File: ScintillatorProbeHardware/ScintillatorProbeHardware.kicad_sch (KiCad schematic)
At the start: 65 parts, among them J1 USB_B, Q1 BUX87, Q2 Q_NPN_BCE, Q3 Q_NPN_BCE, T1 24:1800, U1 ICL7660, U2 LM4562, U3 LM358, U4 STM32F103C8Tx

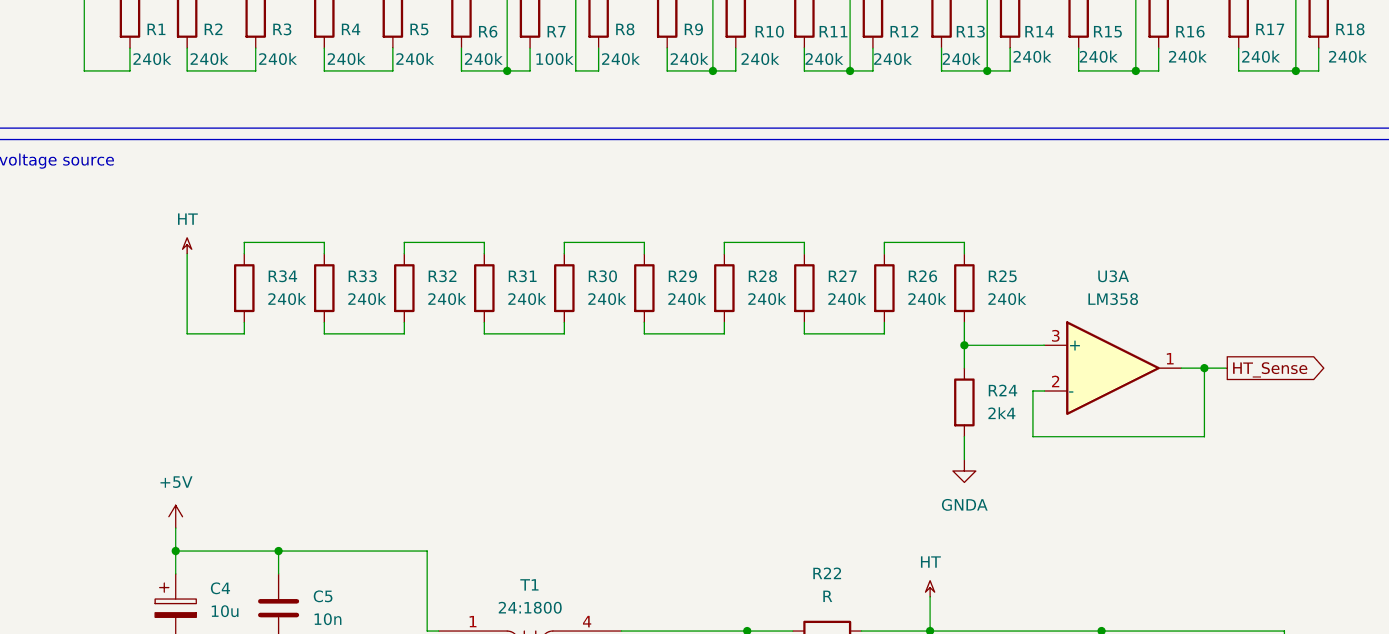
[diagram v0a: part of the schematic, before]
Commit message: USB interface working; Command parser; PWM generator
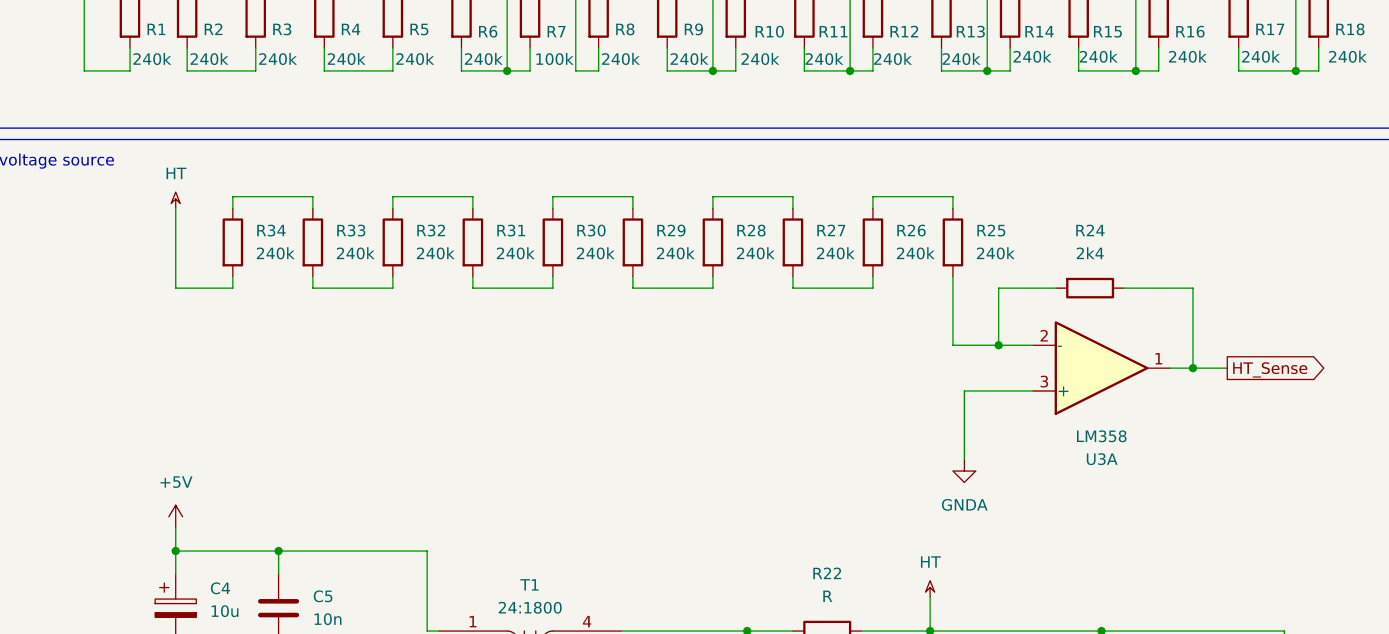
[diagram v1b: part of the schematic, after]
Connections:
- net GNDA: now also U3.3 (+); no longer R24.2
- net HT_Sense: now also R24.1; no longer U3.2 (-)
- new net: R24.2, R25.2, U3.2 (-)
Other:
- moved on the sheet: R24, R25, R26, R27, R28, R29, R30, R31, R32, R33, R34, U3A

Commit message: ...
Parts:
- removed Q2: Q_NPN_BCE, symbol Device:Q_NPN_BCE
- added Q2: BC546A, symbol Device:Q_NPN_CBE
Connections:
- net at R35.2: now also Q2.2 (B)
- net at Q1.2 (C), T1.2 (AB): now also Q2.1 (C)
- net at Q1.1 (B): now also Q2.3 (E)
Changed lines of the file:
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@@
 	)
 	(symbol
-		(lib_id "Device:Q_NPN_BCE")
-		(at 55.88 152.4 0)
-		(unit 1)
-		(exclude_from_sim no)
-		(in_bom yes)
-		(on_board yes)
-		(dnp no)
-		(fields_autoplaced yes)
-		(property "Reference" "Q2"
-			(at 60.96 151.1299 0)
-			(effects
-				(font
-					(size 1.27 1.27)
-				)
-				(justify left)
-			)
-		)
-		(property "Value" "Q_NPN_BCE"
-			(at 60.96 153.6699 0)
-			(effects
-				(font
-					(size 1.27 1.27)
-				)
-				(justify left)
-			)
-		)
-		(property "Footprint" ""
-			(at 60.96 149.86 0)
-			(effects
-				(font
-					(size 1.27 1.27)
-				)
-				(hide yes)
-			)
-		)
-		(property "Datasheet" "~"
-			(at 55.88 152.4 0)
-			(effects
-				(font
-					(size 1.27 1.27)
-				)
-				(hide yes)
-			)
-		)
-		(property "Description" "NPN transistor, base/collector/emitter"
-			(at 55.88 152.4 0)
-			(effects
-				(font
-					(size 1.27 1.27)
-				)
-				(hide yes)
-			)
-		)
-		(pin "3"
-		)
-		(pin "1"
-		)
-		(pin "2"
-		)
-		(instances
-			(project ""
-				(path "/b577c016-7a5f-4050-822e-6f81bc7c5cda"
-					(reference "Q2")
-					(unit 1)
-				)
-			)
-		)
-	)
-	(symbol
 		(lib_id "Amplifier_Operational:LM4562")
 		(at 266.7 66.04 0)
@@
 					(unit 1)
 				)
+			)
+		)
+	)
+	(symbol
+		(lib_id "Device:Q_NPN_CBE")
+		(at 55.88 152.4 0)
+		(unit 1)
+		(exclude_from_sim no)
+		(in_bom yes)
+		(on_board yes)
+		(dnp no)
+		(fields_autoplaced yes)
+		(property "Reference" "Q2"
+			(at 60.96 151.1299 0)
+			(effects
+				(font
+					(size 1.27 1.27)
+				)
+				(justify left)
+			)
+		)
+		(property "Value" "BC546A"
+			(at 60.96 153.6699 0)
+			(effects
+				(font
+					(size 1.27 1.27)
+				)
+				(justify left)
+			)
+		)
+		(property "Footprint" ""
+			(at 60.96 149.86 0)
+			(effects
+				(font
+					(size 1.27 1.27)
+				)
+				(hide yes)
+			)
+		)
+		(property "Datasheet" "~"
+			(at 55.88 152.4 0)
+			(effects
+				(font
+					(size 1.27 1.27)
+				)
+				(hide yes)
+			)
+		)
+		(property "Description" "NPN transistor, collector/base/emitter"
+			(at 55.88 152.4 0)
+			(effects
+				(font
+					(size 1.27 1.27)
+				)
+				(hide yes)
+			)
+		)
+		(pin "1"
+		)
+		(pin "2"
+		)
+		(pin "3"
+		)
+		(instances
+			(project ""
+				(path "/b577c016-7a5f-4050-822e-6f81bc7c5cda"
+					(reference "Q2")
+					(unit 1)
+				)

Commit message: Flyback driving circuit changed to NMOS
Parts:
- removed Q1: BUX87, symbol Device:Q_NPN_BCE
- added D5, D6: D_Schottky, symbol Device:D_Schottky
- added Q1: Q_NMOS_GDS, symbol Device:Q_NMOS_GDS
- added R37: 330R, symbol Device:R
- added R38: 1k, symbol Device:R
- C8: value C -> 1n
- R35: value R -> 330R
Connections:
- net +3.3V: now also D5.1 (K), R37.1
- net GND: now also Q2.3 (E), Q1.3 (S)
- net GNDA: now also D6.2 (A)
- net HT_Sense: now also D5.2 (A), D6.1 (K), R38.2; no longer R24.1, U3.1
- net at Q2.1 (C): now also Q1.1 (G), R37.2; no longer T1.2 (AB)
- new net: R24.1, R38.1, U3.1
- new net: Q1.2 (D), T1.2 (AB)
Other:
- moved on the sheet: Q2, R35

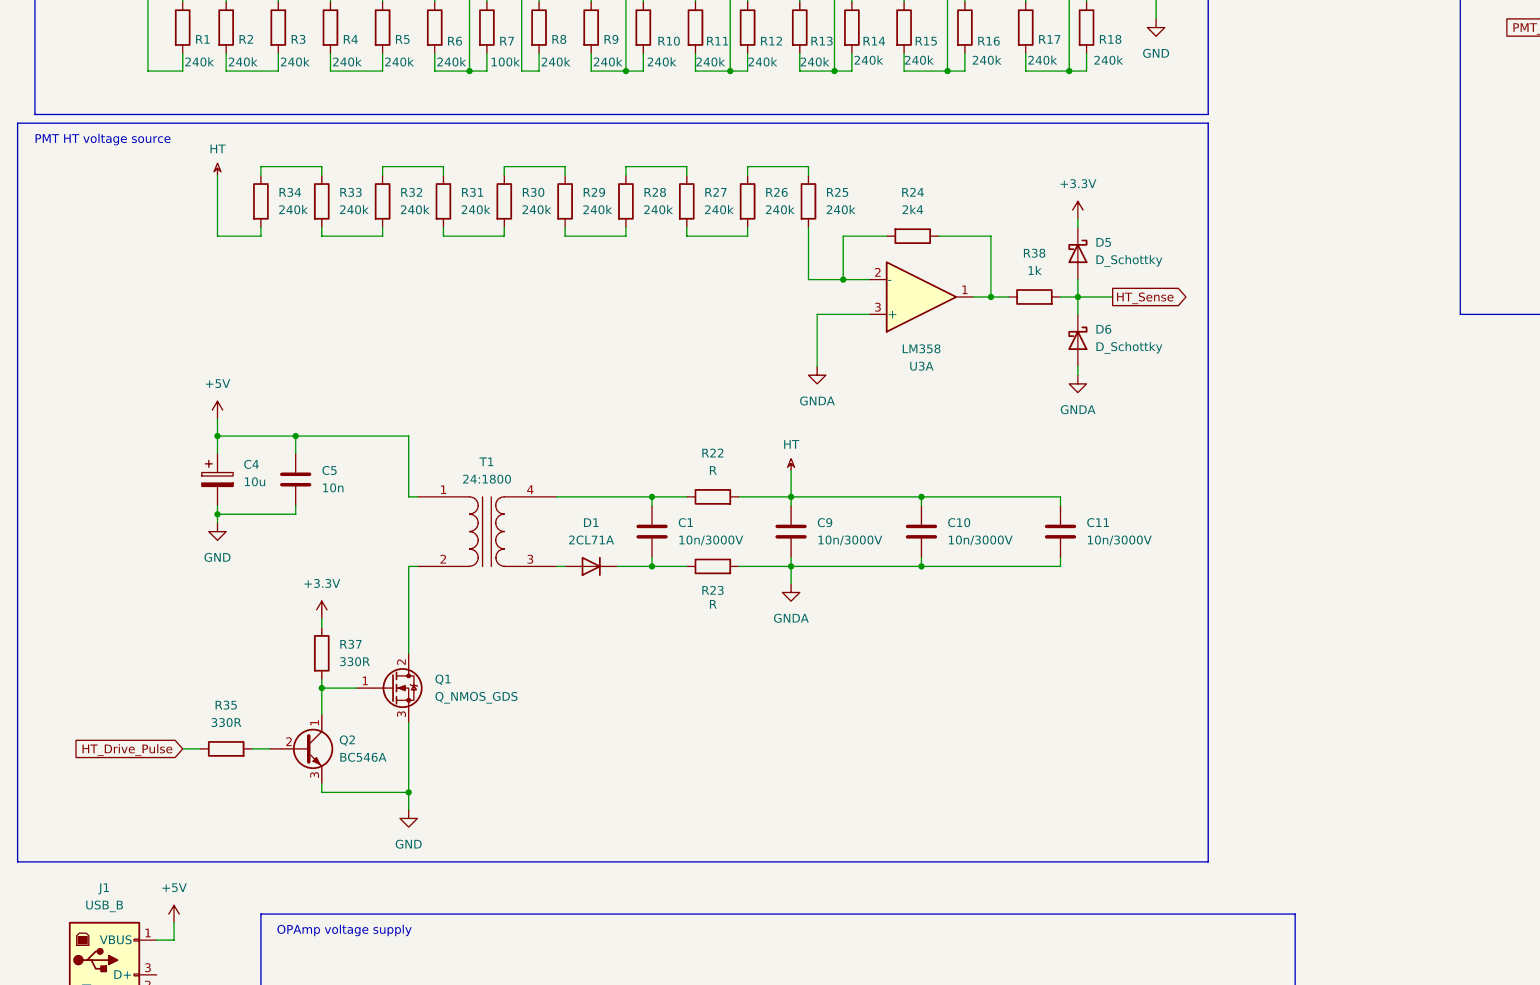
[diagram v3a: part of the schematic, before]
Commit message: Added some LCSC numbers
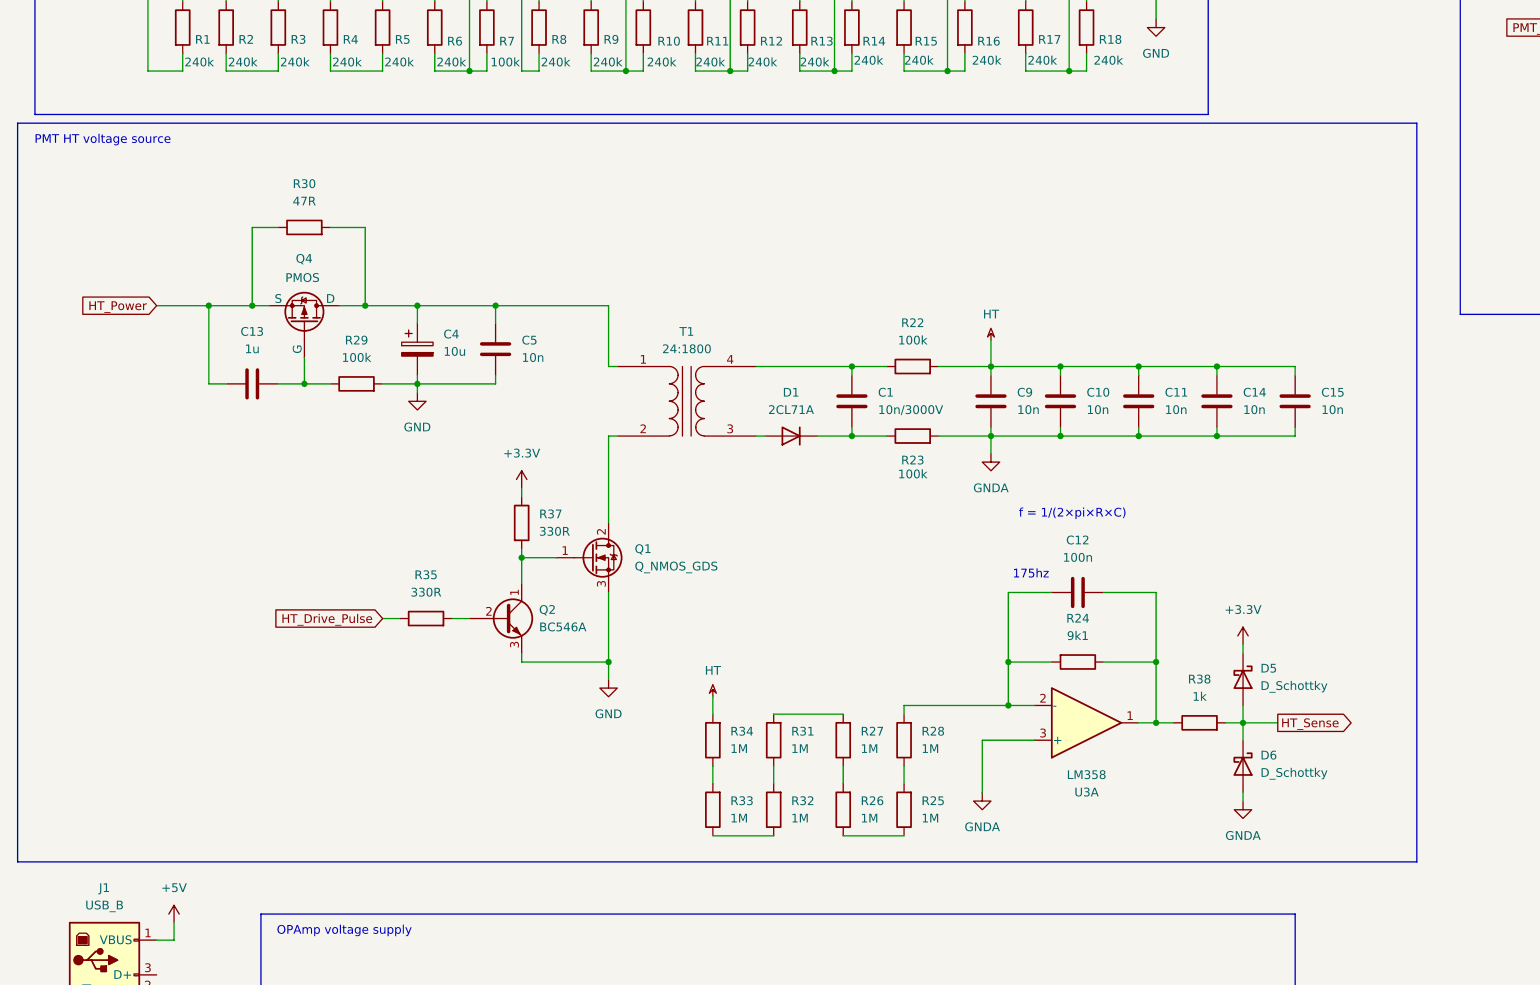
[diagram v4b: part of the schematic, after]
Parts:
- added C12: 100n, Capacitor_SMD:C_0603_1608Metric, symbol Device:C
- added C13: 1u, symbol Device:C
- added C14, C15: 10n, symbol Device:C
- added Q4: PMOS, symbol Simulation_SPICE:PMOS
- C10, C11, C9: value 10n/3000V -> 10n
- R22, R23: value R -> 100k
- R24: value 2k4 -> 9k1; footprint (none) -> Resistor_SMD:R_0603_1608Metric; LCSC (none) -> https://www.lcsc.com/product-detail/Chip-Resistor-Surface-M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; LCSC Part Number (none) -> C23260
- R25, R26, R27, R28, R31, R32, R33, R34: value 240k -> 1M; footprint (none) -> Resistor_SMD:R_1206_3216Metric; LCSC (none) -> https://www.lcsc.com/product-detail/Chip-Resistor-Surface-M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; LCSC Part Number (none) -> C2075184
- R29: value 240k -> 100k
- R30: value 240k -> 47R
- R38: footprint (none) -> Resistor_SMD:R_0603_1608Metric; LCSC (none) -> https://www.lcsc.com/product-detail/Chip-Resistor-Surface-M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; LCSC Part Number (none) -> C21190
- U1: footprint (none) -> Package_SO:SOIC-8_3.9x4.9mm_P1.27mm; LCSC (none) -> https://www.lcsc.com/product-detail/Charge-Pumps_RENESAS-IC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; LCSC Part Number (none) -> C7881
- U3: footprint (none) -> Package_SO:SOIC-8_3.9x4.9mm_P1.27mm; LCSC (none) -> https://www.lcsc.com/product-detail/Operational-Amplifier_T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; LCSC Part Number (none) -> C5423
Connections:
- net +5V: no longer C4.1, C5.1, T1.1 (AA)
- net GND: now also R29.2
- net GNDA: now also C14.2, C15.2
- net HT: now also C14.1, C15.1
- net at R24.1, R38.1, U3.1: now also C12.2
- net at R24.2, U3.2 (-): now also R28.2, C12.1; no longer R25.2
- net at R27.1: now also R26.2; no longer R28.1
- net at R27.2: now also R31.2; no longer R26.2
- net at R33.1: now also R32.1; no longer R34.1
- net at R31.1: now also R32.2; no longer R32.1
- net at R30.2: now also C4.1, C5.1, T1.1 (AA), Q4.1 (D); no longer R31.2
- net at R29.1: now also C13.2, Q4.2 (G); no longer R30.1
- net at R33.2: now also R34.1; no longer R32.2
- new net: R25.2, R28.1
- new net HT_Power: C13.1, Q4.3 (S), R30.1
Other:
- note added: "175hz"
- note added: "f = 1/(2×pi×R×C)"
- moved on the sheet: C1, C10, C11, C4, C5, C9, D1, D5, D6, Q1, Q2, R22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

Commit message: added transformer model; experiments with beeping code
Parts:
- removed D4: D_Schottky, symbol Device:D_Schottky
- removed Q3: Q_NPN_BCE, symbol Device:Q_NPN_BCE
- removed R36: R, symbol Device:R
- removed RV1: R_Potentiometer, symbol Device:R_Potentiometer
- removed unit 1 of U2
- removed unit 2 of U2
- removed unit 2 of U3
- added C16: 1000u, Capacitor_SMD:CP_Elec_10x10.5, symbol Device:C_Polarized
- added C17, C18, C26: 100n, Capacitor_SMD:C_0603_1608Metric, symbol Device:C
- added C19, C20, C21: 10u, Capacitor_SMD:CP_Elec_4x5.4, symbol Device:C_Polarized
- added C22, C23, C24, C25: 20p, Capacitor_SMD:C_0603_1608Metric, symbol Device:C
- added FB4: 620Ω@1MHz, Inductor_SMD:L_1210_3225Metric, symbol Device:FerriteBead
- added J2: Conn_01x02, Connector_PinHeader_2.54mm:PinHeader_1x02_P2.54mm_Vertical, symbol Connector_Generic:Conn_01x02
- added J3: Conn_01x03, Connector_PinHeader_2.54mm:PinHeader_1x03_P2.54mm_Vertical, symbol Connector_Generic:Conn_01x03
- added J4: Conn_01x04, symbol Connector_Generic:Conn_01x04
- added Q3, Q5, Q6: 2N2222A, symbol Device:Q_NPN_CBE
- added U5: USBLC6-2SC6, Package_TO_SOT_SMD:SOT-23-6, symbol Power_Protection:USBLC6-2SC6
- added U6: AMS1117-3.3, Package_TO_SOT_SMD:SOT-223-3_TabPin2, symbol Regulator_Linear:AMS1117-3.3
- added U7, U8, U9: LM318N, Package_SO:SOIC-8_3.9x4.9mm_P1.27mm, symbol Amplifier_Operational:LM318N
- added Y1: 32.768kHz, Crystal:Crystal_SMD_SeikoEpson_MC306-4Pin_8.0x3.2mm, symbol Device:Crystal
- added Y2: 8MHz, Crystal:Crystal_SMD_HC49-SD, symbol Device:Crystal
- C13: footprint (none) -> Capacitor_SMD:C_0603_1608Metric; LCSC (none) -> https://www.lcsc.com/product-detail/Multilayer-Ceramic-Capa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; LCSC Part Number (none) -> C15849
- C2, C3, C6, C7: footprint (none) -> Capacitor_SMD:CP_Elec_4x5.4; LCSC (none) -> https://www.lcsc.com/product-detail/Aluminum-Electrolytic-C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; LCSC Part Number (none) -> RVT1V100M0405
- C4: value 10u -> 1000u; footprint (none) -> Capacitor_SMD:CP_Elec_10x10.5; LCSC (none) -> https://www.lcsc.com/product-detail/Aluminum-Electrolytic-C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; LCSC Part Number (none) -> C5162355
- C5: value 10n -> 10u; footprint (none) -> Capacitor_SMD:C_0805_2012Metric; LCSC (none) -> https://www.lcsc.com/product-detail/Multilayer-Ceramic-Capa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; LCSC Part Number (none) -> C1713
- C8: value 1n -> 10n
- D5, D6: footprint (none) -> Diode_SMD:D_SOD-523; LCSC (none) -> https://www.lcsc.com/product-detail/Schottky-Diodes_onsemi-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; LCSC Part Number (none) -> C145179
- FB1, FB2, FB3: value FerriteBead -> 620Ω@1MHz; footprint (none) -> Inductor_SMD:L_1210_3225Metric; LCSC (none) -> https://www.lcsc.com/product-detail/Ferrite-Beads_Murata-El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; LCSC Part Number (none) -> C2661807
- Q1: value Q_NMOS_GDS -> 15N10; footprint (none) -> Package_TO_SOT_SMD:TO-252-2; LCSC (none) -> https://www.lcsc.com/product-detail/MOSFETs_UMW-Youtai-Semi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; LCSC Part Number (none) -> C359106
- Q2: value BC546A -> S8050; footprint (none) -> Package_TO_SOT_SMD:SOT-23; LCSC (none) -> https://www.lcsc.com/product-detail/Bipolar-BJT_Guangdong-H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; LCSC Part Number (none) -> C181158
- Q4: value PMOS -> AO401; footprint (none) -> Package_TO_SOT_SMD:SOT-23; LCSC (none) -> https://www.lcsc.com/product-detail/MOSFETs_TWGMC-AO3401_C7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; LCSC Part Number (none) -> C727156
- R1, R2: value 240k -> 620k; footprint Resistor_SMD:R_0603_1608Metric -> Resistor_SMD:R_1218_3246Metric; LCSC (none) -> https://www.lcsc.com/product-detail/Chip-Resistor-Surface-M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; LCSC Part Number (none) -> C3014189
- R10, R11, R12, R13, R14, R15, R16, R17, R18, R6, R9: footprint Resistor_SMD:R_0603_1608Metric -> Resistor_SMD:R_1206_3216Metric; LCSC (none) -> https://www.lcsc.com/product-detail/Chip-Resistor-Surface-M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; LCSC Part Number (none) -> C2907378
- R19: value 10k -> 1k
- R20: value 100k -> 10k
- R21: value 1M -> 330R
- R22: value 100k -> 47k; footprint (none) -> Resistor_SMD:R_0805_2012Metric; LCSC (none) -> https://www.lcsc.com/product-detail/Chip-Resistor-Surface-M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; LCSC Part Number (none) -> C102018
- R23: value 100k -> 330R
- R29: footprint (none) -> Resistor_SMD:R_0603_1608Metric; LCSC (none) -> https://www.lcsc.com/product-detail/Chip-Resistor-Surface-M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; LCSC Part Number (none) -> 0603
- R3: value 240k -> 47k; footprint Resistor_SMD:R_0603_1608Metric -> Resistor_SMD:R_0805_2012Metric; LCSC (none) -> https://www.lcsc.com/product-detail/Chip-Resistor-Surface-M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; LCSC Part Number (none) -> C102018
- R30: footprint (none) -> Resistor_SMD:R_2010_5025Metric; LCSC (none) -> https://www.lcsc.com/product-detail/Chip-Resistor-Surface-M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; LCSC Part Number (none) -> C2960940
- R35: value 330R -> 1k
- R37: footprint (none) -> Resistor_SMD:R_1812_4532Metric; LCSC (none) -> https://www.lcsc.com/product-detail/Chip-Resistor-Surface-M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; LCSC Part Number (none) -> C2933950
- R4: value 240k -> 330R; footprint Resistor_SMD:R_0603_1608Metric -> Resistor_SMD:R_1812_4532Metric; LCSC (none) -> https://www.lcsc.com/product-detail/Chip-Resistor-Surface-M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; LCSC Part Number (none) -> C2933950
- R5: value 240k -> 10k; LCSC (none) -> https://www.lcsc.com/product-detail/Chip-Resistor-Surface-M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; LCSC Part Number (none) -> C25804
- R7: value 100k -> 336k; footprint Resistor_SMD:R_0603_1608Metric -> Resistor_SMD:R_1206_3216Metric; LCSC (none) -> https://www.lcsc.com/product-detail/Chip-Resistor-Surface-M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; LCSC Part Number (none) -> C407275
- R8: value 240k -> 1k; footprint Resistor_SMD:R_0603_1608Metric -> (none)
- T1: footprint (none) -> CustomParts:15kV_Transformer
- U4: LCSC (none) -> https://www.lcsc.com/product-detail/Microcontrollers-MCU-MP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; LCSC Part Number (none) -> C8734
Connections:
- net +3.3V: now also D6.1 (K), R5.2, U4.24 (VDD), U4.36 (VDD), U4.48 (VDD), C20.1, FB4.1, J3.1 (Pin_1), J4.1 (Pin_1), U6.2 (VO); no longer D5.1 (K), R37.1
- net +5V: now also C19.1, U5.5 (VBUS), U6.3 (VI)
- net +5VA: now also C17.2, C18.2, Q3.1 (C), U7.7 (V+), U8.7 (V+), U9.7 (V+)
- net -5V: now also FB3.1; no longer FB2.1
- net -5VA: now also FB3.2, C17.1, C18.1, U7.4 (V-), U8.4 (V-), U9.4 (V-); no longer FB2.2
- net GND: now also FB2.1, U4.23 (VSS), U4.35 (VSS), U4.47 (VSS), C16.2, C19.2, C20.2, C22.1, C23.1, C24.1, C25.1, C26.1, J2.1 (Pin_1), J3.3 (Pin_3), J4.4 (Pin_4), U5.2 (GND), U6.1 (GND); no longer D3.2 (A), FB3.1
- net GNDA: now also C8.1, D3.2 (A), D5.2 (A), FB2.2, R3.1, R8.2, U4.8 (VSSA), C21.2, Q5.3 (E), Q6.3 (E), U8.3 (+); no longer C8.2, D6.2 (A), FB3.2, R23.2
- net HT_Drive_Pulse: now also R4.1; no longer R35.1
- net HT_Sense: now also D5.1 (K), D6.2 (A); no longer D5.2 (A), D6.1 (K)
- net PMT_Anode: now also R8.1, U7.3 (+); no longer R20.1
- net Peak_Reset: now also R21.1, R23.2
- net Peak_Sense: now also D2.2 (A), D3.1 (K), R35.2
- net at R20.2: now also Q3.2 (B), Q6.1 (C), U8.6; no longer R21.1
- net at R21.2: now also Q5.2 (B); no longer D2.2 (A)
- net at R19.1: now also U7.2 (-), U7.6
- net at R6.1, V1.16 (Modulator), V1.2 (D1): now also R2.2; no longer R5.1
- net +3.3VA: now reaches D2.1 (K)
- net +3.3VA: now also U4.9 (VDDA), C21.1, FB4.2; no longer C8.1
- net at C4.1, C5.1, Q4.1 (D)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: now also R37.1, C16.1
- net at R4.2: now also Q2.2 (B); no longer R5.2
- net at R7.1: now also R9.1, V1.3 (D3); no longer R8.2
- net at C1.2, D1.1 (K): now also R3.2; no longer R23.1
- net at J1.2 (D-): now also U5.3 (I/O2)
- net at J1.3 (D+): now also U5.1 (I/O1)
- net at U4.2 (PC13): now also C22.2, Y2.2
- net at U4.3 (PC14): now also C23.2, Y2.1
- net USB_D-: now reaches U4.32 (PA11)
- net USB_D-: now also U5.4 (I/O2)
- net USB_D+: now reaches U4.33 (PA12)
- net USB_D+: now also U5.6 (I/O1)
- net SWDIO: now reaches U4.34 (PA13)
- net SWDIO: now also J4.3 (Pin_3)
- net SWCLK: now reaches U4.37 (PA14)
- net SWCLK: now also J4.2 (Pin_2)
- net BOOT0: now reaches U4.44 (BOOT0)
- net BOOT0: now also J3.2 (Pin_2)
- net at U4.5 (PD0): now also C24.2, Y1.2
- net at U4.6 (PD1): now also C25.2, Y1.1
- net at U4.7 (NRST): now also R5.1, C26.2, J2.2 (Pin_2)
- net Pulse_Trigger: no longer names the net of R19.2
- net Pulse_Trigger: now also R20.1, U8.2 (-); no longer D3.1 (K)
- new net: C8.2, Q3.3 (E), Q5.1 (C), U9.3 (+)
- new net: Q6.2 (B), R23.1
- new net: R35.1, U9.2 (-), U9.6
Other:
- moved on the sheet: C13, C2, C3, C4, C5, C6, C7, FB1, J1, Q4, R1, R29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
